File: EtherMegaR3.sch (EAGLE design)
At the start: 115 parts, among them IC1 EUP3476SO08T, IC2 APX811-44UG-7, IC3 ATMEGA8U2-MU, IC6 W5100SQFP80, IC9 ATMEGA2560-16AU, J1 DC_2_1MM, P1 USB-FT, P3 ICSP:USB, P4 microSD, Q2 2N7002, Q3 2N7002, U1 HY931147C-RJ45, X1 16MHz, X2 25MHz, X3 16MHz

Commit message: Changes for R3 release
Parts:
- C6: value 47uF 25V -> 47uF 50V 1210 ceramic; device rcl:CPOL-EUD -> freetronics-jon:C-EUC1210
- IC3: value ATMEGA8U2-MU -> ATMEGA16U2-MU
- P1: value USB-FT -> USB-6PSMT; device freetronics-master-v1:USB-FT -> freetronics-jon:USB-6PSMT
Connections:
- removed net N$9: L3.1, P1.SH$1, P1.SH$2, P1.SH$3, P1.SH$4, Z1.2, Z2.2
- new net N$18: L3.1, P1.FIX1, P1.FIX2, P1.PIN1, P1.PIN2, P1.TAB1, P1.TAB2, Z1.2, Z2.2
- new net NC: JP6.8
- net 5V: now also C6.2, JP6.7; no longer C6.+
- net GND: now also C6.1; no longer C6.-
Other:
- note added: "ATmega16U2 Microcontroller"
- note added: "V2.0 (2012-08-18)"
- note removed: "ATmega8U2 Microcontroller"
- note removed: "V1.1 (2011-10-26)"
- moved on the sheet: C1, C27, C32, C35, C36, C37, IC1, L4, R10, R11, R12, R9

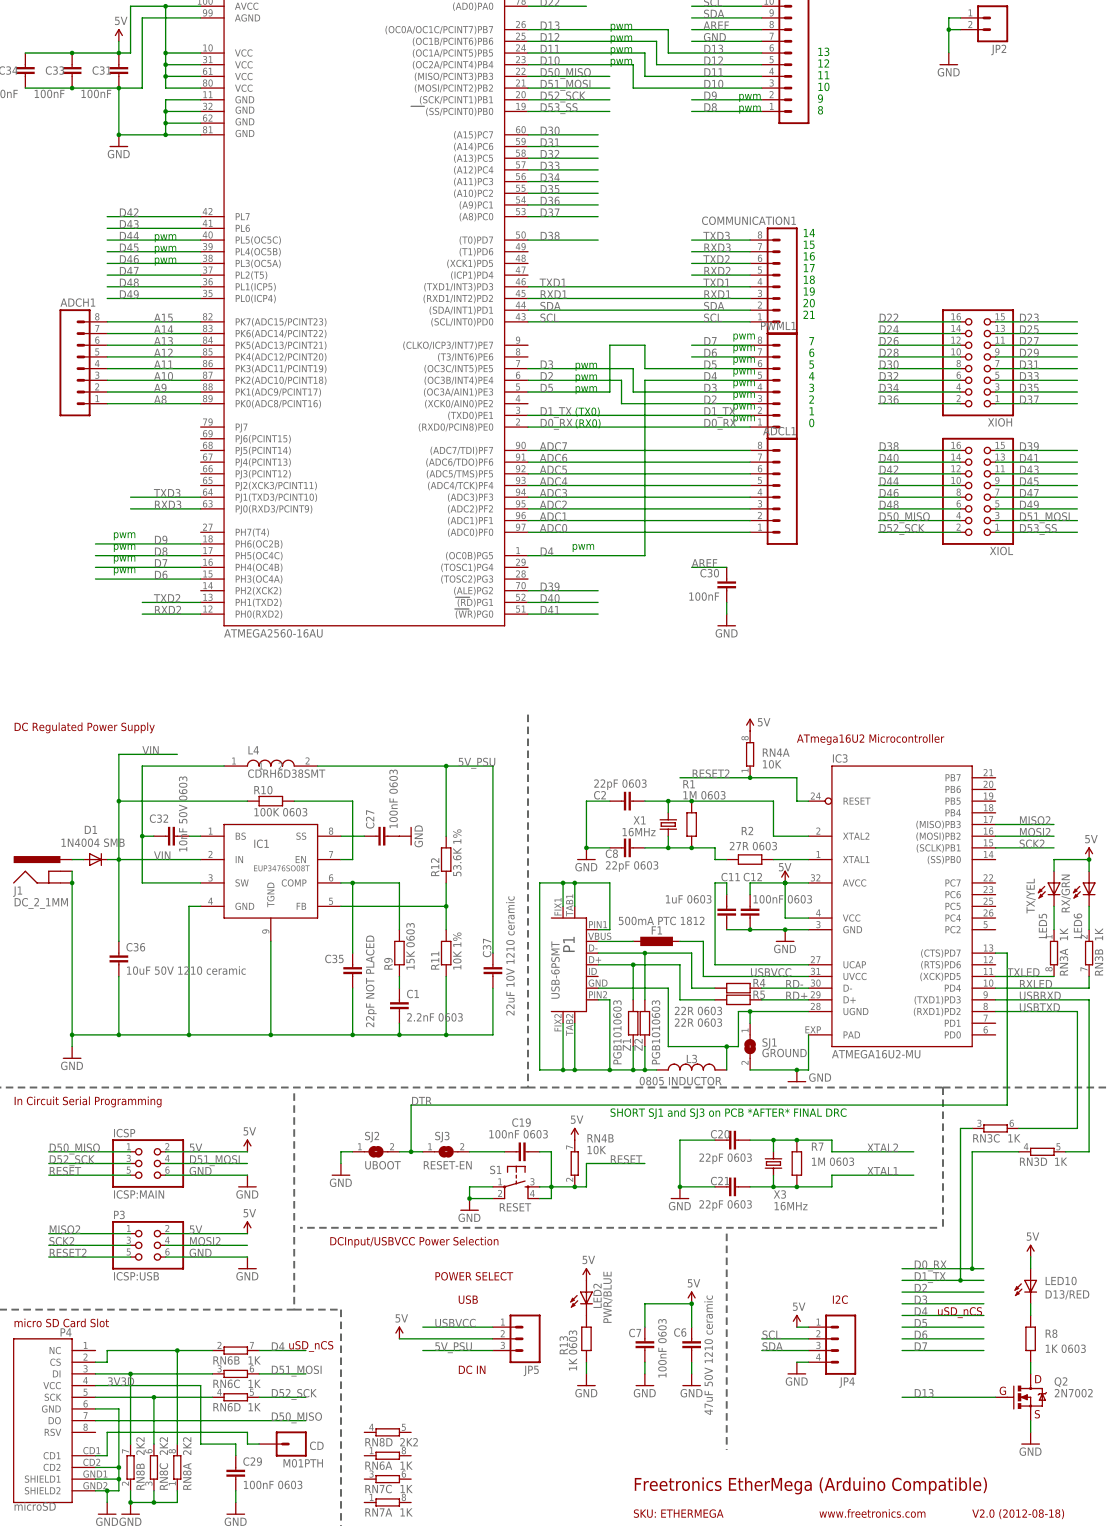
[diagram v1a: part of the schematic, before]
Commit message: Added MAC address chip and changed to hinge SD socket for v3.0 release
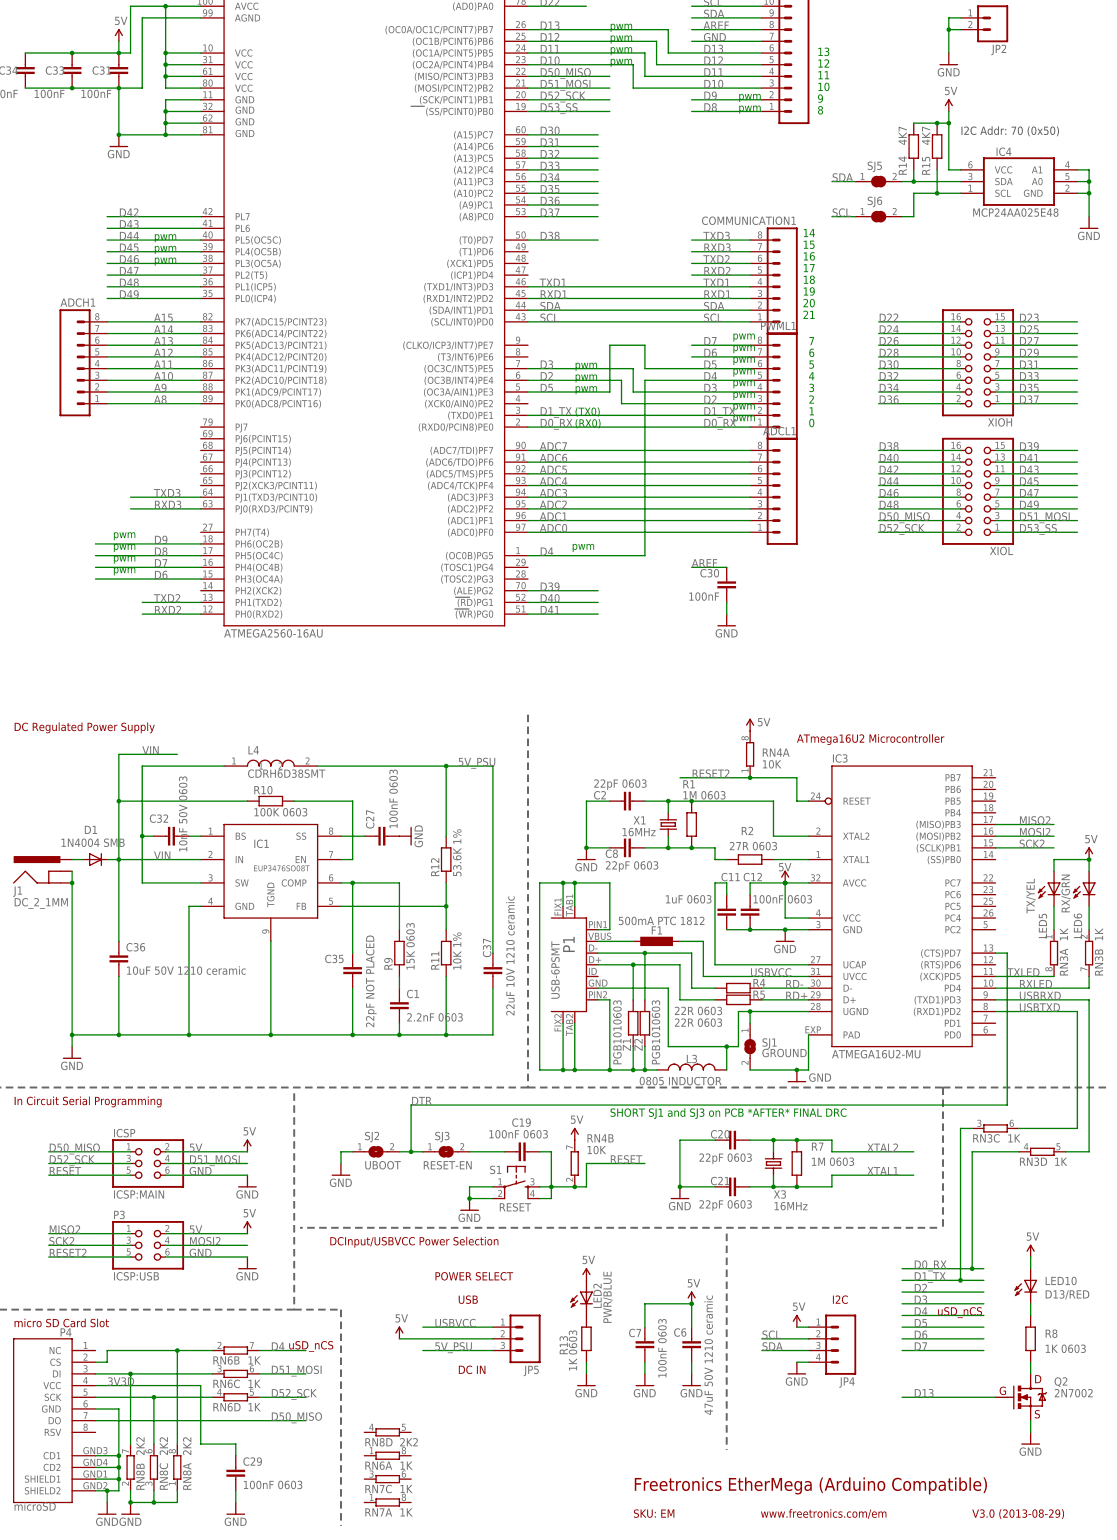
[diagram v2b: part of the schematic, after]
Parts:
- removed CD: M01PTH, freetronics-2:M01PTH
- added IC4: MCP24AA025E48, freetronics-jon:MCP24AA025E48
- added R14, R15: 4K7, freetronics-master-v1.1:RESISTOR0603
- added SJ5, SJ6: SJCN, freetronics-jon:SJCN
- LED1, LED10, LED2, LED3, LED4, LED5, LED6, LED7, LED8, LED9: device freetronics:LED0603 -> freetronics-jon:LED0603
- P4: device freetronics-master-v1:USD-SOCKETNEW -> freetronics-jon:USD-SOCKETHINGE
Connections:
- removed net N$23: CD.1, P4.CD1
- new net N$19: IC4.SDA, R14.2, SJ5.2
- new net N$9: IC4.SCL, R15.2, SJ6.2
- net 5V: now also IC4.VCC, R14.1, R15.1
- net GND: now also IC4.A0, IC4.A1, IC4.GND, P4.CD1
- net SCL: now also SJ6.1
- net SDA: now also SJ5.1
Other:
- note added: "I2C Addr: 70 (0x50)"
- note added: "SKU: EM"
- note added: "V3.0 (2013-08-29)"
- note added: "www.freetronics.com/em"
- note removed: "SKU: ETHERMEGA"
- note removed: "V2.0 (2012-08-18)"
- note removed: "www.freetronics.com"

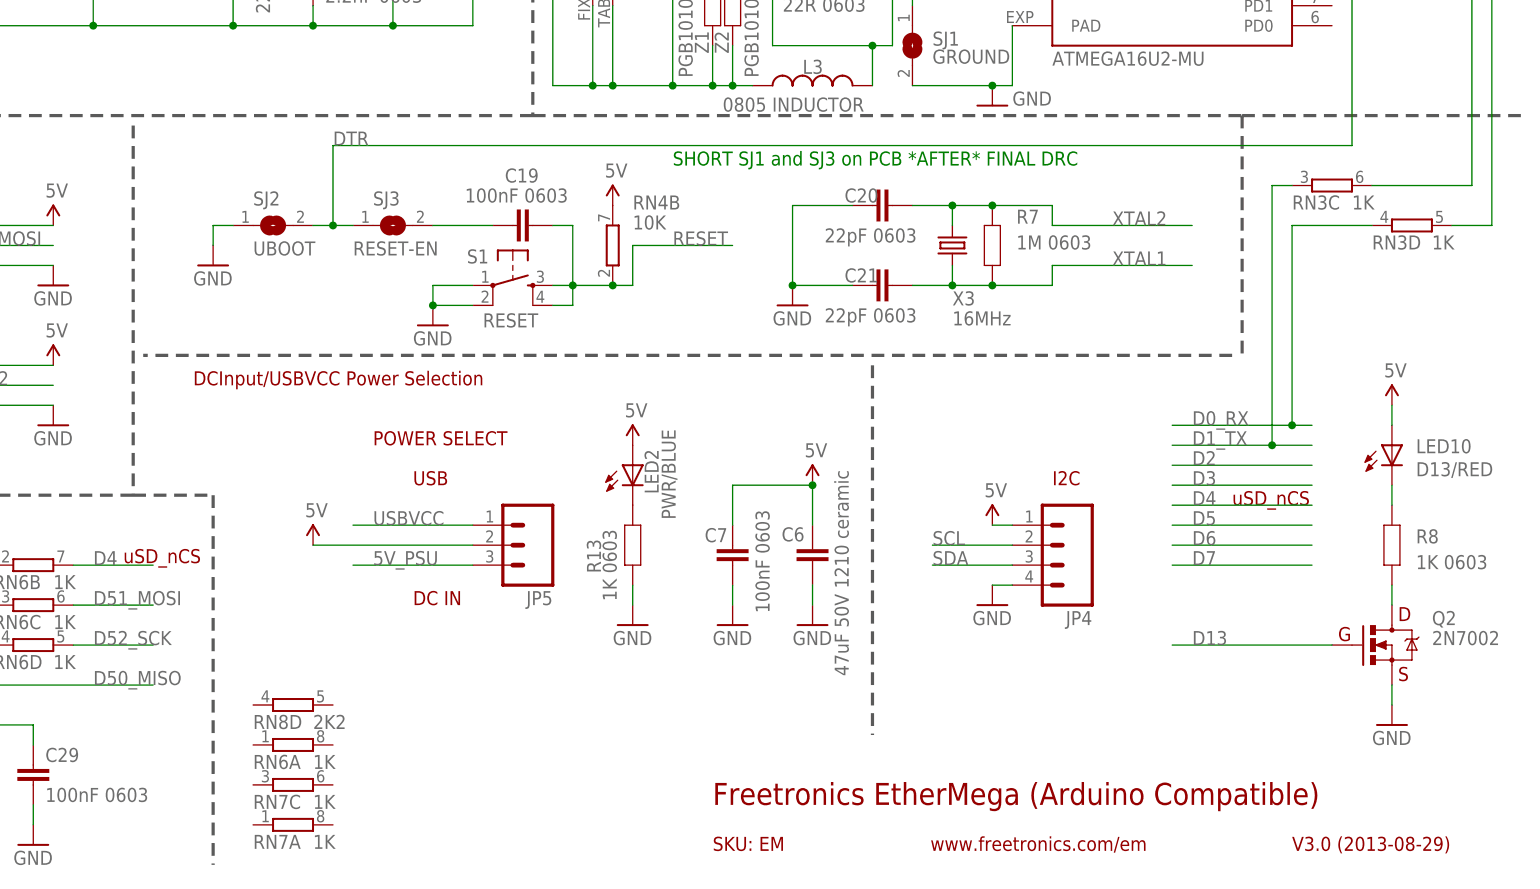
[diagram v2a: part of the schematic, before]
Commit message: Added M02 header in parallel with RST-EN cut-track link for external reset mode control
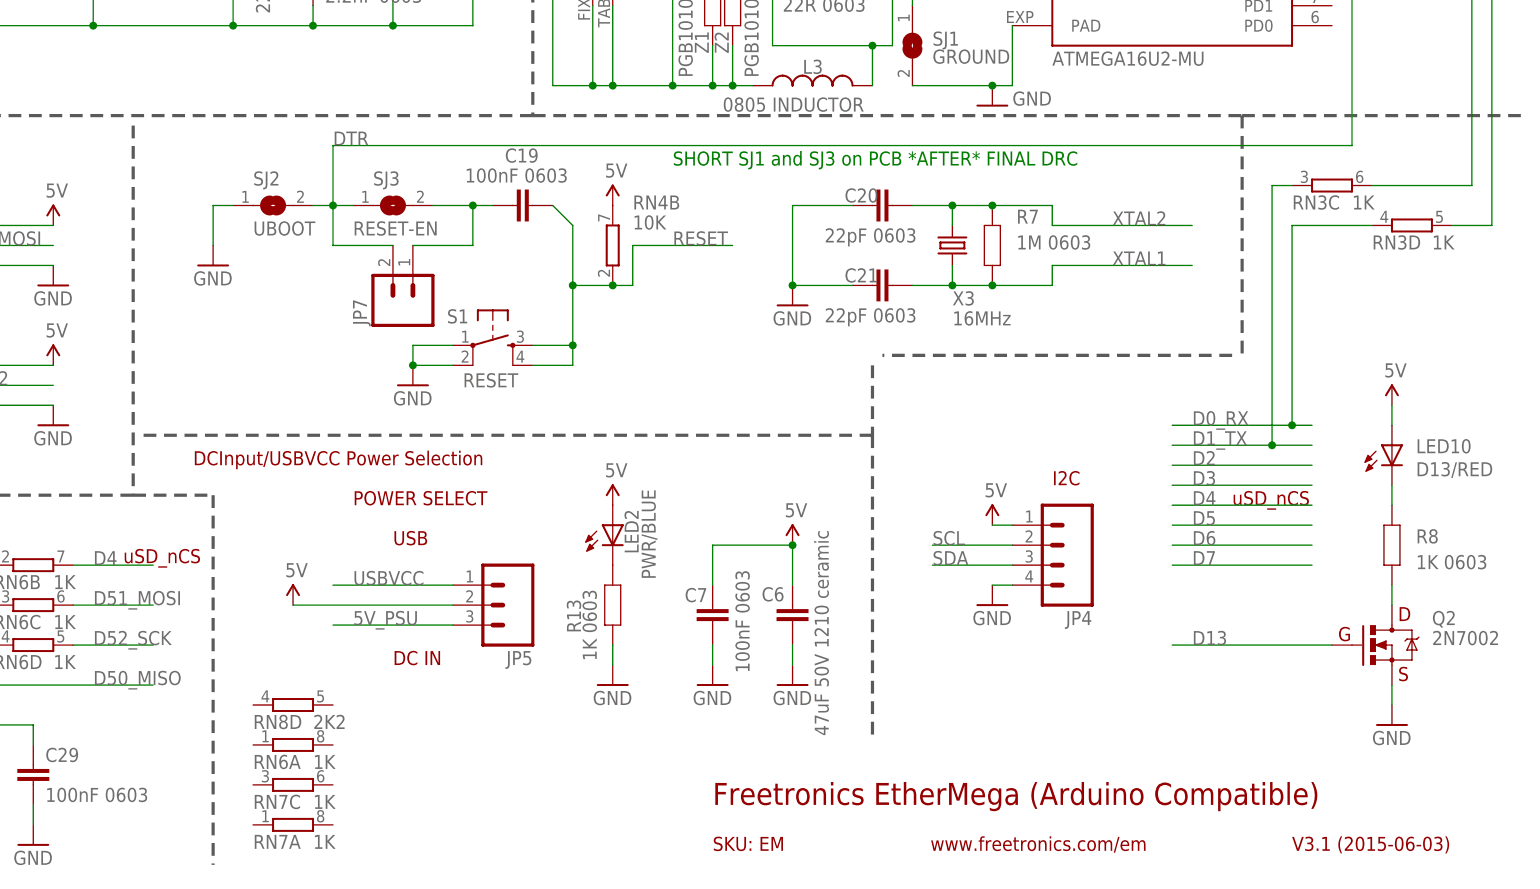
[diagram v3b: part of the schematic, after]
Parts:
- added JP7: (no value), freetronics-master-v1.1:M02PTH
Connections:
- net DTR: now also JP7.2
- net N$75: now also JP7.1
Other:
- note added: "V3.1 (2015-06-03)"
- note removed: "V3.0 (2013-08-29)"
- moved on the sheet: C19, C6, C7, JP5, LED2, R13, S1, SJ2, SJ3
